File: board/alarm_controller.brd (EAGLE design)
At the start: 90 x 65 mm, 146 parts, among them IC3 AT24C, X1 RJ45-8L21-S, X2 RJ45-8L21-S

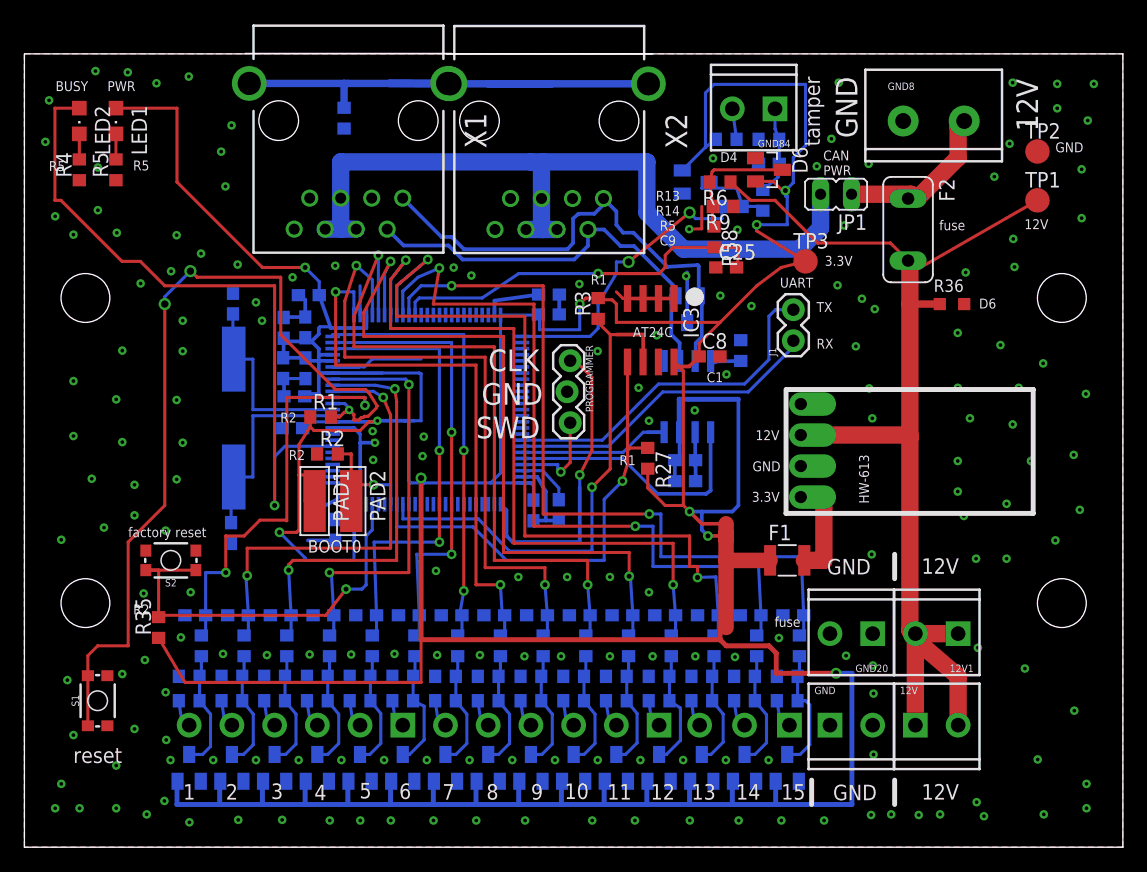
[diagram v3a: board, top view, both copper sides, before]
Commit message: jumpers for boot mode
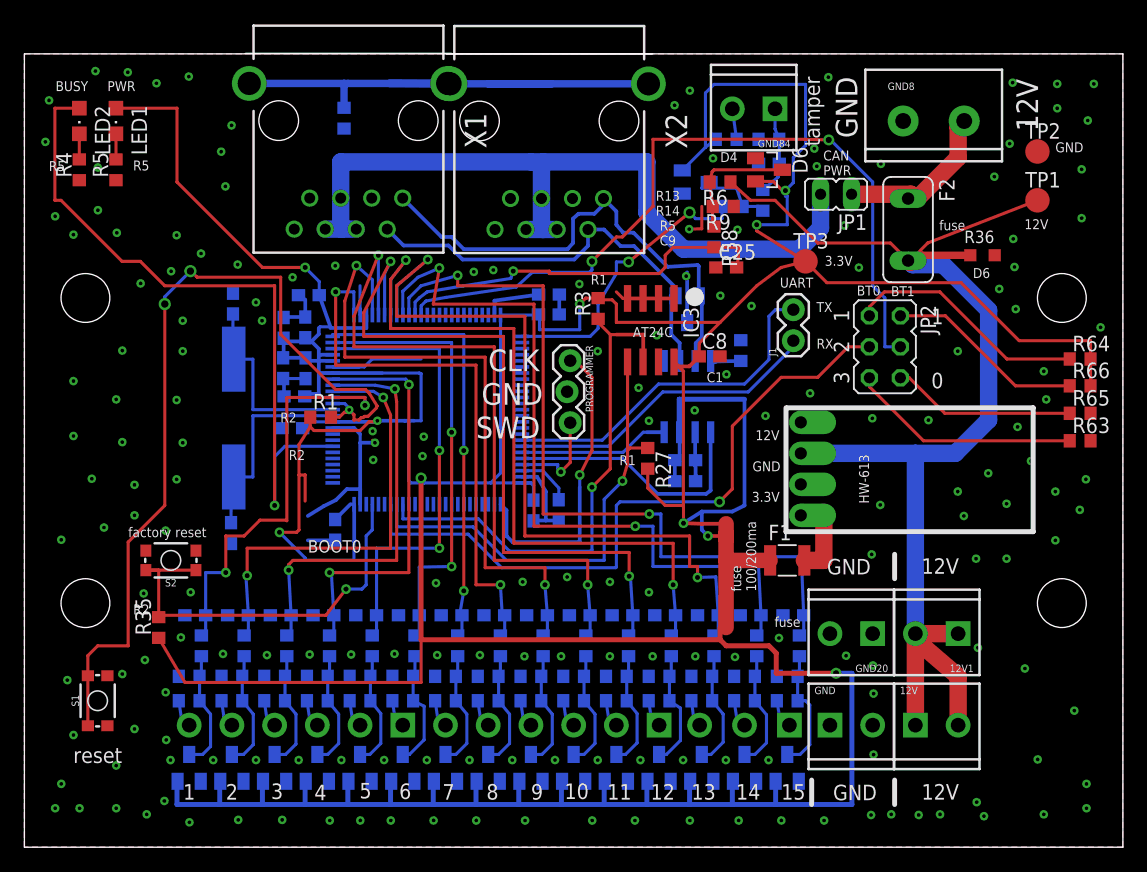
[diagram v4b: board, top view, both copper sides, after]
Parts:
- removed PAD1, PAD2: WIREPADSMD5-1,8, wirepad:5-1,8
- removed R2: 10k, rcl:R0603
- added JP2: (no value), jumper:JP3Q
- added R63, R64, R65, R66: 10k, rcl:R0603
- moved R36 4.72 mm to (78.5, 48.5)
- moved U$4 1.50 mm to (72.5, 31.0)
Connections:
- removed net N$12: PAD2.1, R2.2, U$1.BOOT0
- new net BOOT0: JP2.3, U$1.BOOT0
- new net BOOT1: JP2.4, U$1.PB2
- new net N$13: JP2.1, R64.1
- new net N$14: JP2.6, R65.1
- new net N$15: JP2.5, R63.1
- new net N$5: JP2.2, R66.1
- net +3V3: now also R64.2, R66.2; no longer PAD1.1
- net GND: now also R63.2, R65.2; no longer R2.1
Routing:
- net BOOT1: track 0.00 -> 63.4 mm, vias 0 -> 2
- net BOOT0: track 0.00 -> 56.3 mm, vias 0 -> 1
- net +3V3: track 457.5 -> 489.0 mm
- net N$13: track 0.00 -> 19.9 mm
- net N$15: track 0.00 -> 19.0 mm
- net N$5: track 0.00 -> 16.3 mm
- net N$14: track 0.00 -> 15.1 mm
- net +12V: track 91.6 -> 103.6 mm
- net N$12: track 9.80 -> 0.00 mm, vias 1 -> 0
- net ALARM_15: track 63.0 -> 63.9 mm
- net N$3: track 8.68 -> 7.75 mm
- net GND: vias 184 -> 185
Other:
- board text added: "0"
- board text added: "BT0"
- board text added: "BT1"
- board text added: "fuse 100/200ma"

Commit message: fix labels
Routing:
- net +3V3: track 489.0 -> 486.3 mm
- net GND: vias 185 -> 189
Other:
- board text added: "alarm controller 2020.07.18 v1.3"
- board text removed: "alarm controller 2020.06.11 v1.3"
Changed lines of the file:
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@@
 <text x="7.915" y="45.3134" size="1.524" layer="200" font="vector">alarm
 controller
-2020.06.11
+2020.07.18
 v1.3</text>
 <rectangle x1="5.3298" y1="22.7654" x2="5.6854" y2="22.8162" layer="200"/>
@@
 <text x="59.95" y="20.95" size="0.8128" layer="121" rot="R90">fuse
 100/200ma</text>
+<text x="83.3" y="39.65" size="0.8128" layer="121">R2</text>
+<text x="83.4" y="32.85" size="0.8128" layer="121">R2</text>
+<text x="83.3" y="37.4" size="0.8128" layer="121">R2</text>
+<text x="83.35" y="35.1" size="0.8128" layer="121">R2</text>
 </plain>
 <attributes>
@@
 <via x="54.52" y="61.99" extent="1-16" drill="0.3" diameter="0.3048"/>
 <via x="53.27" y="60.79" extent="1-16" drill="0.3" diameter="0.3048"/>
+<via x="23.3256" y="30.0836" extent="1-16" drill="0.3"/>
+<via x="23.5756" y="26.8336" extent="1-16" drill="0.3"/>
+<via x="27.2756" y="30.1336" extent="1-16" drill="0.3"/>
+<via x="27.0756" y="32.1336" extent="1-16" drill="0.3"/>
 </signal>
 <signal name="+3V3">
@@
 <wire x1="32.5" y1="38.8" x2="32.35" y2="38.85" width="0.254" layer="16"/>
 <wire x1="32.35" y1="38.85" x2="29.31" y2="38.85" width="0.254" layer="16"/>
-<wire x1="23" y1="28.36" x2="23" y2="30.5" width="0.254" layer="1"/>
-<wire x1="23" y1="30.5" x2="22.5" y2="30.5" width="0.254" layer="1"/>
-<wire x1="22.5" y1="30.5" x2="22.5" y2="33" width="0.254" layer="1"/>
 <wire x1="22.5" y1="33" x2="23.42" y2="34.44" width="0.254" layer="1"/>
 <wire x1="59" y1="36.7" x2="59" y2="28" width="0.3048" layer="16"/>
@@
 <wire x1="27" y1="25.02" x2="27" y2="23.5" width="0.254" layer="16"/>
 <wire x1="27" y1="23.5" x2="23" y2="23.5" width="0.254" layer="16"/>
-<wire x1="22.5" y1="30.5" x2="22.5" y2="26" width="0.254" layer="1"/>
+<wire x1="22.5" y1="33" x2="22.5" y2="26" width="0.254" layer="1"/>
 <wire x1="22.5" y1="26" x2="22.3" y2="25.8" width="0.254" layer="1"/>
 <wire x1="22.3" y1="25.8" x2="20.9" y2="25.8" width="0.254" layer="1"/>

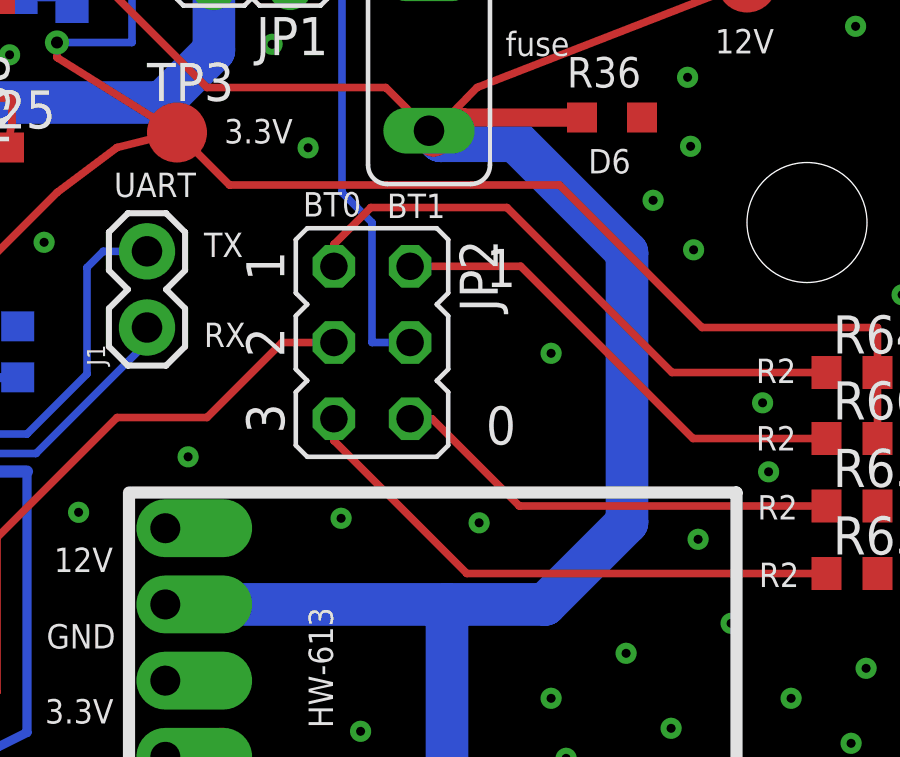
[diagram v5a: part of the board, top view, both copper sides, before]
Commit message: change to solderable boot jumper
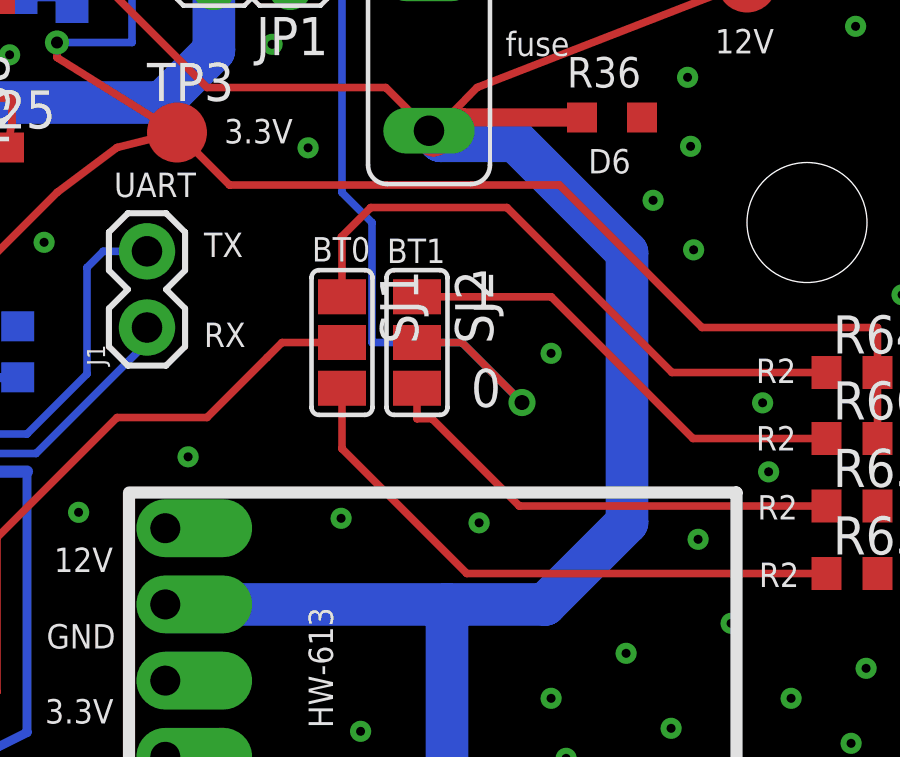
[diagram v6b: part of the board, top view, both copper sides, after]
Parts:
- removed JP2: (no value), jumper:JP3Q
- added SJ1, SJ2: (no value), jumper:SJ_2
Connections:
- net BOOT0: now also SJ1.2; no longer JP2.3
- net BOOT1: now also SJ2.2; no longer JP2.4
- net N$13: now also SJ1.1; no longer JP2.1
- net N$14: now also SJ2.3; no longer JP2.6
- net N$15: now also SJ1.3; no longer JP2.5
- net N$5: now also SJ2.1; no longer JP2.2
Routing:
- net BOOT1: track 63.4 -> 72.3 mm, vias 2 -> 3
- net N$13: track 19.9 -> 20.9 mm
- net N$15: track 19.0 -> 19.9 mm
- net N$14: track 15.1 -> 15.9 mm
- net N$5: track 16.3 -> 15.6 mm
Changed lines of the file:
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@@
 <text x="73.5" y="22.4" size="1.27" layer="121">12V</text>
 <text x="65.75" y="22.35" size="1.27" layer="121">GND</text>
-<text x="68.2" y="45.2" size="0.8128" layer="121">BT0</text>
-<text x="71" y="45.15" size="0.8128" layer="121">BT1</text>
-<text x="74.3" y="42.85" size="1.27" layer="121">1</text>
-<text x="74.3" y="37.6" size="1.27" layer="121">0</text>
+<text x="68.5" y="43.7" size="0.8128" layer="121">BT0</text>
+<text x="71" y="43.65" size="0.8128" layer="121">BT1</text>
+<text x="73.7" y="42.1" size="1.27" layer="121">1</text>
+<text x="73.8" y="38.85" size="1.27" layer="121">0</text>
 <text x="59.95" y="20.95" size="0.8128" layer="121" rot="R90">fuse
 100/200ma</text>
@@
 <element name="R65" library="rcl" package="R0603" value="10k" x="86.5" y="35.55"/>
 <element name="R66" library="rcl" package="R0603" value="10k" x="86.5" y="37.8"/>
-<element name="JP2" library="jumper" package="JP3Q" value="" x="70.5" y="41" rot="R270"/>
+<element name="SJ1" library="jumper" package="SJ_2" value="" x="69.5" y="41" rot="R270"/>
+<element name="SJ2" library="jumper" package="SJ_2" value="" x="72" y="41" rot="R270"/>
 </elements>
 <signals>
@@
 <wire x1="65.9" y1="57.95" x2="63.95" y2="58" width="0.254" layer="1"/>
 <wire x1="63.95" y1="58" x2="51.5" y2="58" width="0.254" layer="1"/>
-<contactref element="JP2" pad="4"/>
-<wire x1="70.5" y1="41" x2="71.77" y2="41" width="0.254" layer="16"/>
+<contactref element="SJ2" pad="2"/>
+<wire x1="70.5" y1="41" x2="73.5" y2="41" width="0.254" layer="16"/>
+<wire x1="73.5" y1="41" x2="75.5" y2="39" width="0.254" layer="16"/>
+<via x="75.5" y="39" extent="1-16" drill="0.5"/>
+<wire x1="75.5" y1="39" x2="73.5" y2="41" width="0.254" layer="1"/>
+<wire x1="73.5" y1="41" x2="72" y2="41" width="0.254" layer="1"/>
 </signal>
 <signal name="BOOT0">
@@
 <wire x1="36.35" y1="25.65" x2="39.1" y2="22.9" width="0.254" layer="16"/>
 <wire x1="39.1" y1="22.9" x2="48.45" y2="22.9" width="0.254" layer="16"/>
-<contactref element="JP2" pad="3"/>
 <wire x1="48.45" y1="22.9" x2="48.5" y2="22.95" width="0.254" layer="16"/>
 <wire x1="48.5" y1="22.95" x2="48.5" y2="28" width="0.254" layer="16"/>
@@
 <wire x1="58" y1="34.5" x2="62" y2="38.5" width="0.254" layer="1"/>
 <wire x1="62" y1="38.5" x2="65" y2="38.5" width="0.254" layer="1"/>
-<wire x1="65" y1="38.5" x2="67.5" y2="41" width="0.254" layer="1"/>
-<wire x1="67.5" y1="41" x2="69.23" y2="41" width="0.254" layer="1"/>
+<wire x1="65" y1="38.5" x2="67" y2="40.5" width="0.254" layer="1"/>
+<contactref element="SJ1" pad="2"/>
+<wire x1="69.5" y1="41" x2="67.5" y2="41" width="0.254" layer="1"/>
+<wire x1="67.5" y1="41" x2="67" y2="40.5" width="0.254" layer="1"/>
 </signal>
 <signal name="N$5">
 <contactref element="R66" pad="1"/>
-<wire x1="75.46" y1="43.54" x2="81.2" y2="37.8" width="0.254" layer="1"/>
+<wire x1="76.476" y1="42.524" x2="81.2" y2="37.8" width="0.254" layer="1"/>
 <wire x1="81.2" y1="37.8" x2="85.65" y2="37.8" width="0.254" layer="1"/>
-<contactref element="JP2" pad="2"/>
-<wire x1="75.46" y1="43.54" x2="71.77" y2="43.54" width="0.254" layer="1"/>
+<contactref element="SJ2" pad="1"/>
+<wire x1="72" y1="42.524" x2="76.476" y2="42.524" width="0.254" layer="1"/>
 </signal>
 <signal name="N$13">
@@
 <wire x1="75" y1="45.5" x2="80.5" y2="40" width="0.254" layer="1"/>
 <wire x1="80.5" y1="40" x2="85.65" y2="40" width="0.254" layer="1"/>
-<contactref element="JP2" pad="1"/>
-<wire x1="70.46" y1="45.5" x2="69.23" y2="44.27" width="0.254" layer="1"/>
-<wire x1="69.23" y1="44.27" x2="69.23" y2="43.54" width="0.254" layer="1"/>
+<wire x1="70.46" y1="45.5" x2="69.48" y2="44.52" width="0.254" layer="1"/>
+<contactref element="SJ1" pad="1"/>
+<wire x1="69.5" y1="42.524" x2="69.5" y2="44.5" width="0.254" layer="1"/>
+<wire x1="69.5" y1="44.5" x2="69.48" y2="44.52" width="0.254" layer="1"/>
 </signal>
 <signal name="N$14">
 <contactref element="R65" pad="1"/>
 <wire x1="75.41" y1="35.55" x2="85.65" y2="35.55" width="0.254" layer="1"/>
-<contactref element="JP2" pad="6"/>
 <wire x1="75.41" y1="35.55" x2="72.5" y2="38.46" width="0.254" layer="1"/>
-<wire x1="72.5" y1="38.46" x2="71.77" y2="38.46" width="0.254" layer="1"/>
+<contactref element="SJ2" pad="3"/>
+<wire x1="72.5" y1="38.46" x2="72" y2="38.46" width="0.254" layer="1"/>
+<wire x1="72" y1="38.46" x2="72" y2="39.476" width="0.254" layer="1"/>
 </signal>
 <signal name="N$15">
 <contactref element="R63" pad="1"/>
 <wire x1="73.66" y1="33.3" x2="85.65" y2="33.3" width="0.254" layer="1"/>
-<contactref element="JP2" pad="5"/>
-<wire x1="73.66" y1="33.3" x2="69.23" y2="37.73" width="0.254" layer="1"/>
-<wire x1="69.23" y1="37.73" x2="69.23" y2="38.46" width="0.254" layer="1"/>
+<wire x1="73.66" y1="33.3" x2="69.5" y2="37.46" width="0.254" layer="1"/>
+<contactref element="SJ1" pad="3"/>
+<wire x1="69.5" y1="39.476" x2="69.5" y2="37.46" width="0.254" layer="1"/>
 </signal>
 </signals>

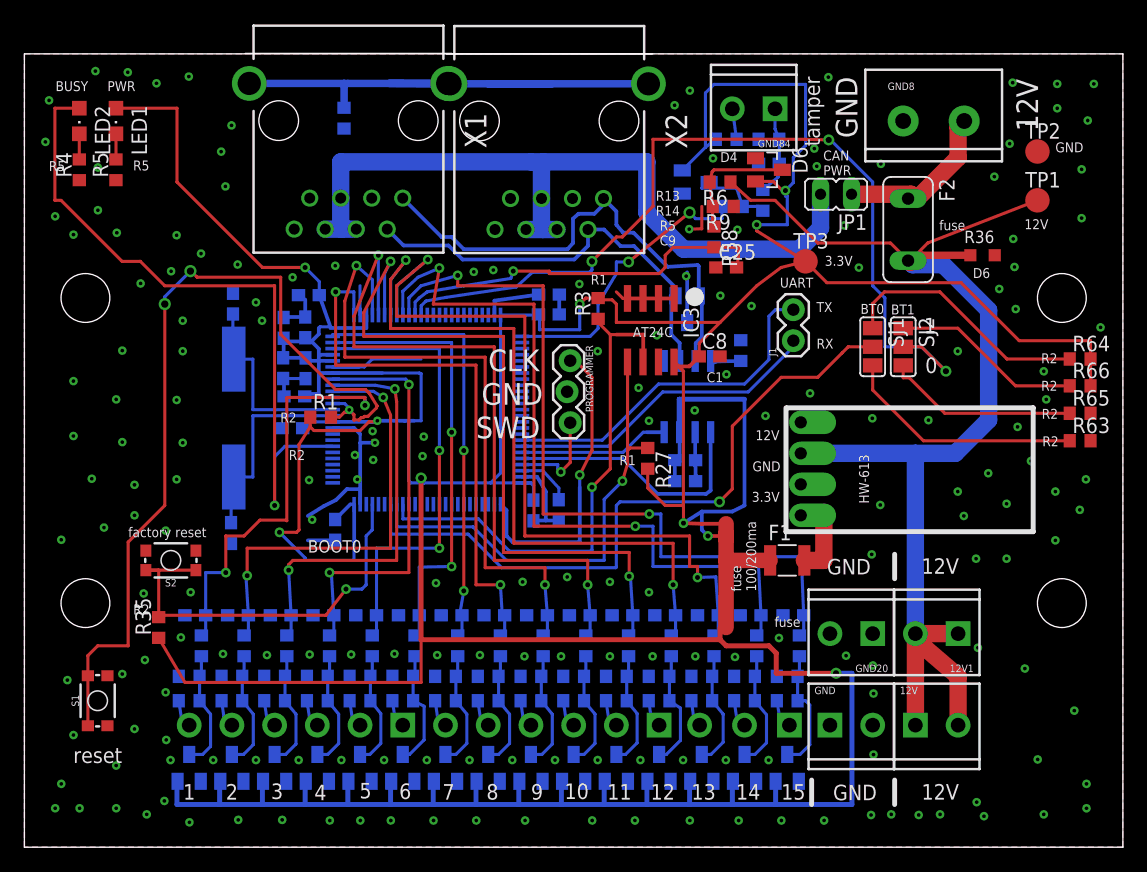
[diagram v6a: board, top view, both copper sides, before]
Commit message: change to microfit from rj45
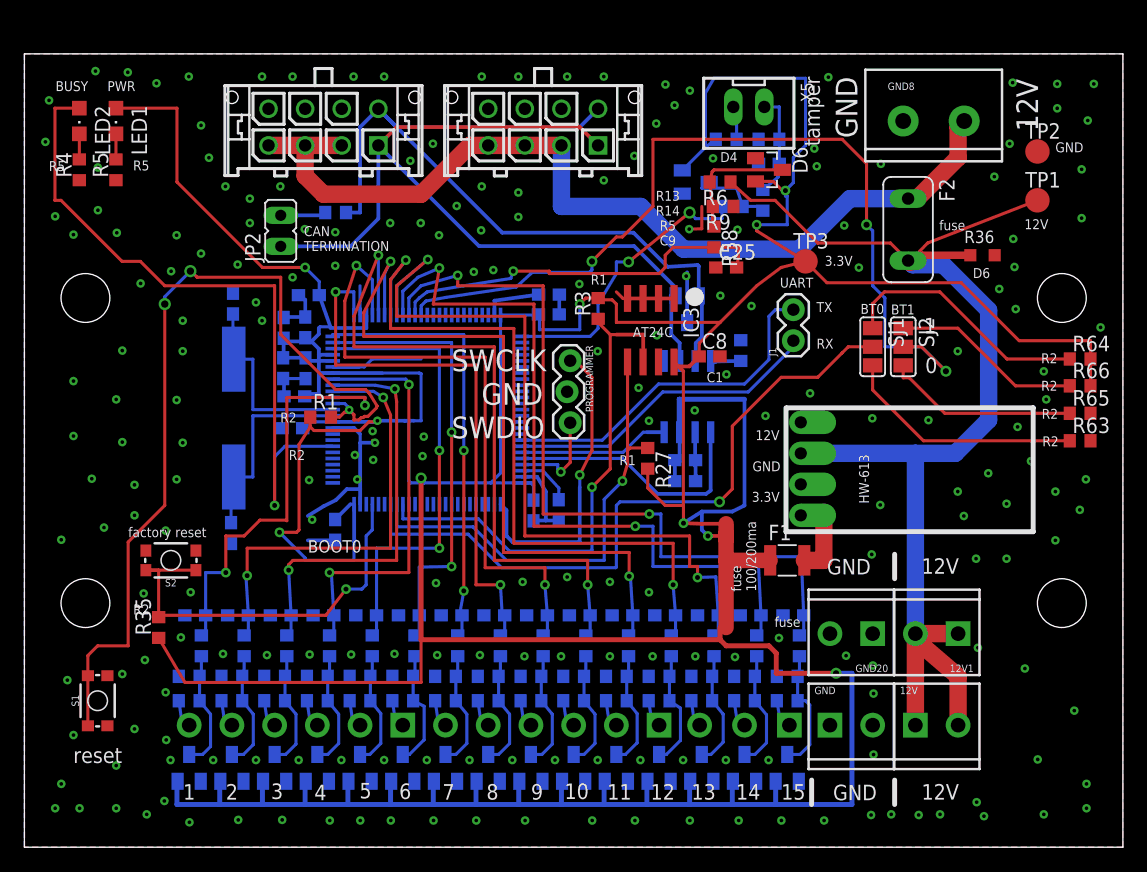
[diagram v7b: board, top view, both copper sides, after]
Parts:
- removed GND84: (no value), SparkFun-Connectors:SCREWTERMINAL-3.5MM-2
- removed JP1: (no value), jumper:JP1
- removed R25: 10k, rcl:R0603
- removed X1, X2: RJ45-8L21-S, con-tycoelectronics:RJ45-SHIELD1
- added JP2: (no value), jumper:JP1
- added R2: 120, rcl:R0603
- added X3, X4: (no value), con-molex-micro-fit-3_0:43045-0812
- added X5: JST-XH-02-PIN-LONG-PAD, Rembrandt Electronics - JST XH Connectors v1-0:JST-XH-02-PACKAGE-LONG-PAD
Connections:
- removed net N$20: R25.1, X1.S1, X1.S2, X2.S1, X2.S2
- removed net RJ45_12V: JP1.2, X1.4, X1.5, X1.6, X2.4, X2.5, X2.6
- new net N$12: JP2.2, R2.1
- net CAN_H: now also R2.2, X3.P$5, X4.P$5; no longer X1.1, X2.1
- net CAN_L: now also JP2.1, X3.P$1, X4.P$1; no longer X1.2, X2.2
- net GND: now also X3.P$6, X3.P$7, X3.P$8, X4.P$6, X4.P$7, X4.P$8; no longer R25.2, X1.3, X1.7, X1.8, X2.3, X2.7, X2.8
- net N$10: now also X5.2; no longer GND84.2
- net N$11: now also X5.1; no longer GND84.1
- net PRE_FUSE_12V: now also X3.P$2, X3.P$3, X3.P$4, X4.P$2, X4.P$3, X4.P$4; no longer JP1.1
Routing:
- net RJ45_12V: track 64.4 -> 0.00 mm
- net PRE_FUSE_12V: track 14.1 -> 77.0 mm
- net N$20: track 49.5 -> 0.00 mm
- net CAN_L: track 35.1 -> 70.0 mm
- net CAN_H: track 40.3 -> 69.3 mm
- net N$12: track 0.00 -> 3.88 mm
- net N$11: track 7.40 -> 8.71 mm
- net +3V3: track 486.3 -> 487.2 mm
- net GND: vias 189 -> 216
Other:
- board text added: "CAN TERMINATION"
- board text added: "R21"
- board text added: "SWCLK"
- board text added: "SWDIO"
- board text added: "alarm controller 2020.08.14 v1.4"
- board text removed: "CAN PWR"
- board text removed: "CLK"
- board text removed: "SHIELD"
- board text removed: "SWD"
- board text removed: "alarm controller 2020.07.18 v1.3"
